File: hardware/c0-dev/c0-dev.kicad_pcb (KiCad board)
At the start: 2 copper layers, 565 parts, among them J1 2913730000, J10 2913730000, J11 2913730000, J12 2913710000, J13 2913730000, J14 2913730000, J15 RJ45_LED_Shielded, J16 TAG_CONNECT, J17 PinHeader_2.54mm, J2 2913710000, J3 2913730000, J4 2913730000, J5 2913710000, J6 2913730000, J7 2913730000, J8 2913710000, J9 2913730000, Q1 BSS138P, Q10 BSS138P, Q2 BSS138P, Q3 BSS138P, Q4 BSS138P, Q5 BSS138P, Q6 BSS138P, Q7 BSS138P, Q8 BSS138P, Q9 BSS138P, U1 LAN8720A, U10 RP2350A, U11 TMP117xxDRV, U12 B0505S-1WR3, U13 ISO1540, U14 AMS1117-3.3, U15 ADS1015IDGS, U16 ADS1015IDGS, U17 B0505S-1WR3, U18 ISO1540, U19 ADS1015IDGS, U2 TPS54360DDA, U20 ADS1015IDGS, U21 ADS1015IDGS, U22 ADS1015IDGS, U23 B0505S-1WR3, U24 ISO6741, U25 ISO6741, U26 ADS1220xPW, U27 ADS1220xPW, U28 B0505S-1WR3, U29 ISO1044BD, U3 TPS2378, U30 TLP175A, U31 ISO1212, U32 ISO1212, U33 ISO1212, U34 ISO1212, U35 B0505S-1WR3, U36 ISO1540, U37 TLP175A, U38 TCA9555PWR, U39 TPS26600PWP, U39 TPS4H000A-Q1, U4 TLP175A, U40 TPS26600PWP, U41 TPS26600PWP, U42 TPS26600PWP, U43 TPS26600PWP, U44 TPS26600PWP, U45 TPS26600PWP, U46 TPS26600PWP, U47 ER_OLEDM0.91_1x-I2C, U47 TPS26600PWP, U48 ER_OLEDM0.91_1x-I2C, U48 TPS4H000A-Q1, U5 B0505S-1WR3, U6 AMS1117-3.3, U7 TCA9555PWR, U8 W25Q128JVP, U9 TPS3820-33DBV, Y1 ABM8-272-T3 (12Mhz)

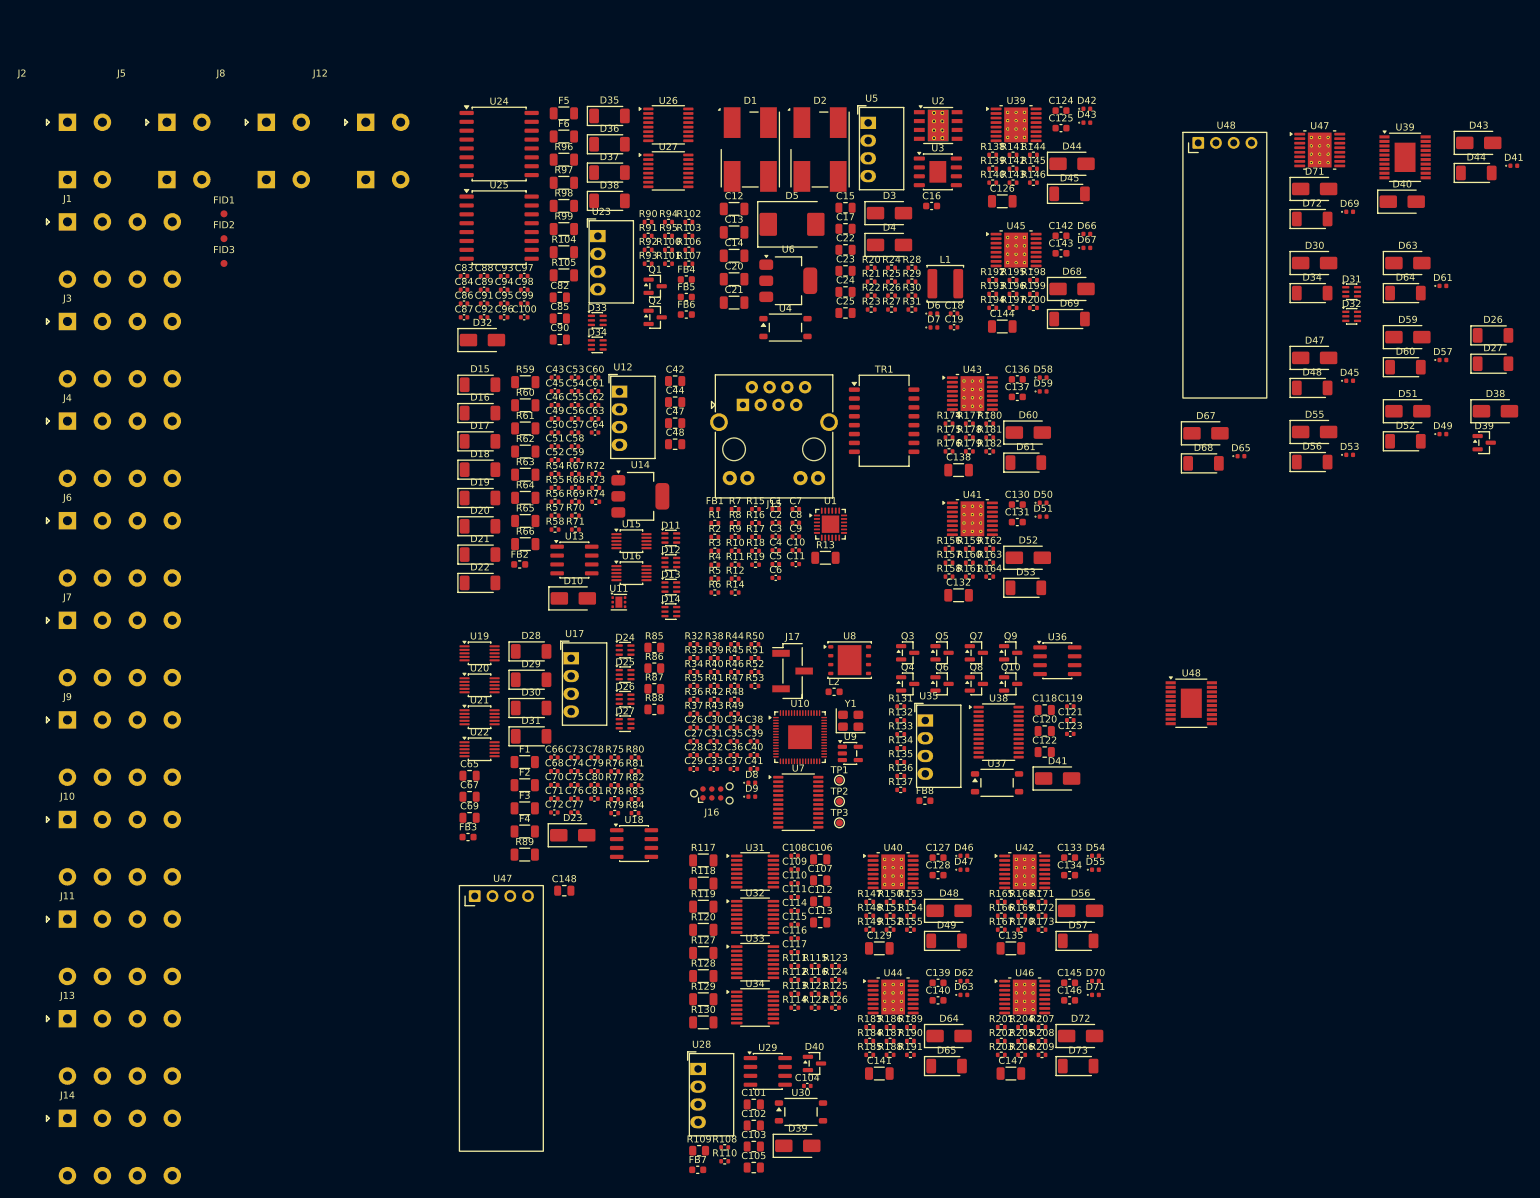
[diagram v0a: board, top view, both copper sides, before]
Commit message: power and isolation cleanup
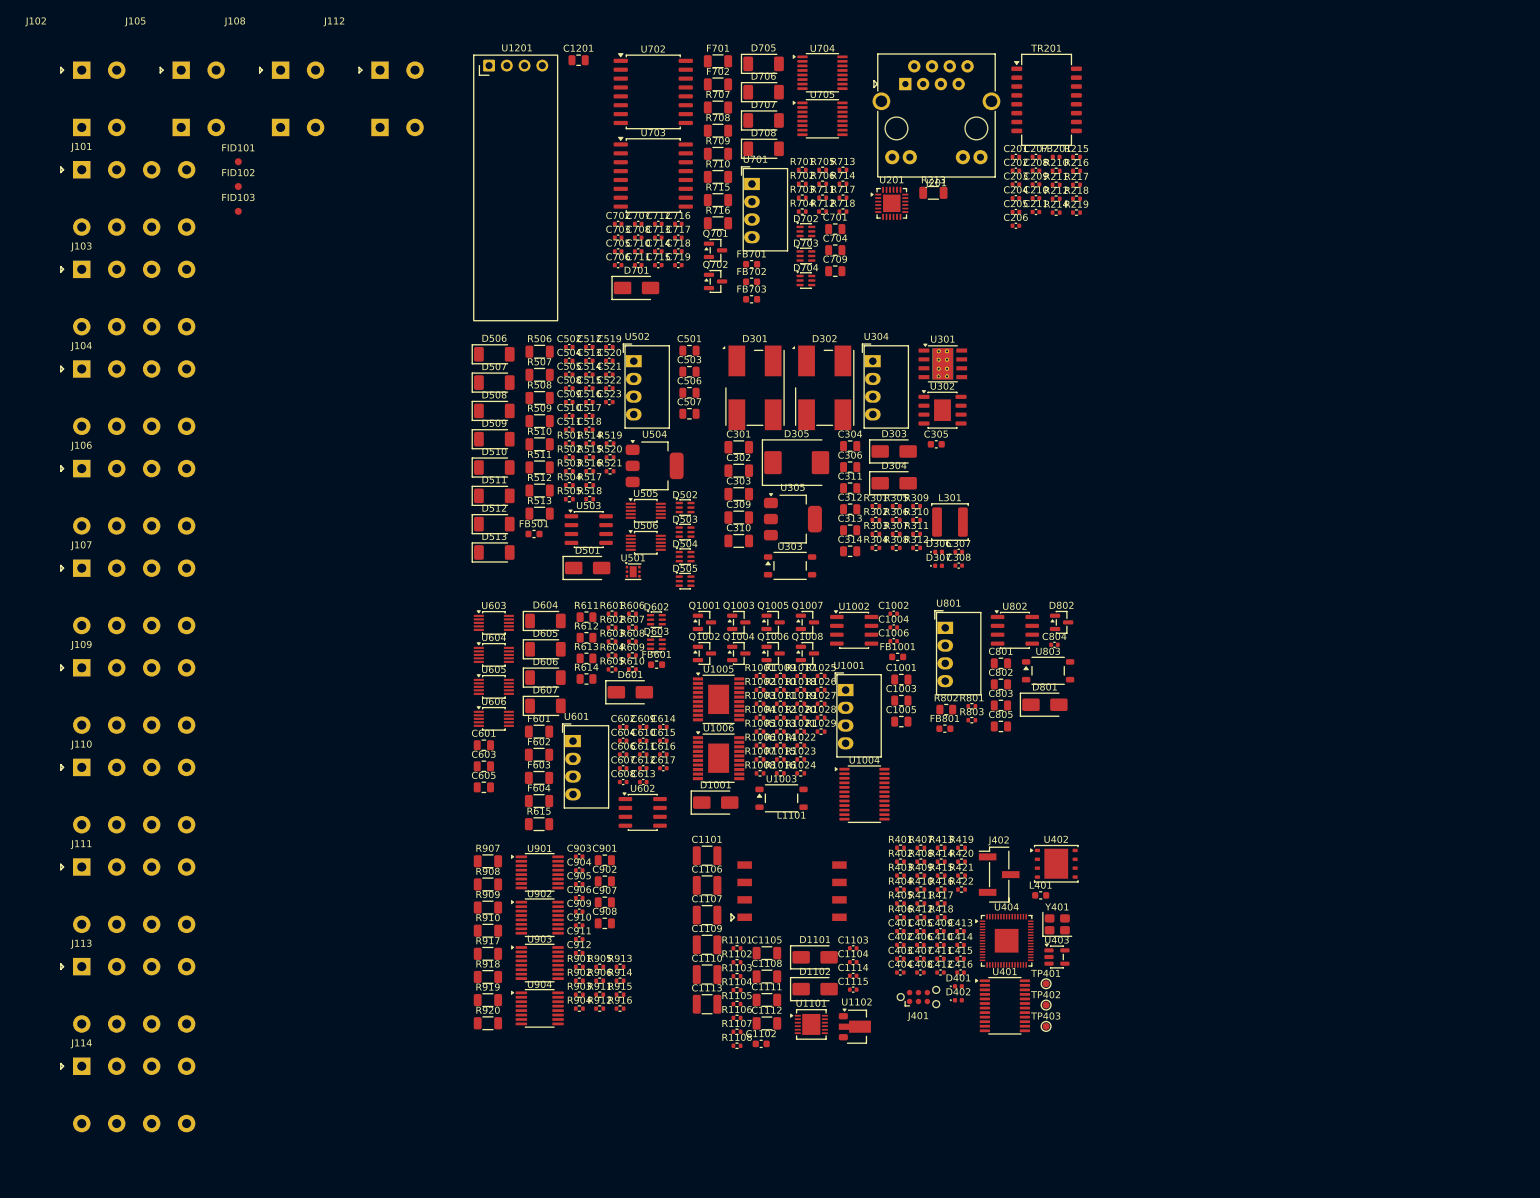
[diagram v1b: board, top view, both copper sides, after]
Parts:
- removed C1, C100, C104, C119, C121, C123, C26, C4, C43, C45, C46, C5, C51, C52, C53, C54, C55, C56, C57, C58, C59, C6, C60, C61, C62, C63, C64, C66, C68, C74, C75, C76, C77, C78, C79, C80, C81, C83, C84, C86, C87, C88, C89, C91, C92, C93, C94, C95, C96, C97, C98, C99: 0.1uF, Capacitor_SMD:C_0402_1005Metric
- removed C10, C11, C7, C8, C9: 22nF, Capacitor_SMD:C_0402_1005Metric
- removed C101, C102, C103, C105, C106, C107, C112, C113, C118, C120, C122, C148, C22, C23, C24, C25, C42, C44, C47, C48, C65, C67, C69, C82, C85, C90: 10uF, Capacitor_SMD:C_0805_2012Metric
- removed C108, C109, C110, C111, C114, C115, C116, C117: 1nF, Capacitor_SMD:C_0402_1005Metric
- removed C12, C13, C14: 1uF, Capacitor_SMD:C_1206_3216Metric
- removed C124, C127, C130, C133, C136, C139, C142, C145: 1uF, Capacitor_SMD:C_0603_1608Metric
- removed C125, C128, C131, C134, C137, C140, C143, C146: 2.2uF, Capacitor_SMD:C_0603_1608Metric
- removed C126, C129, C132, C135, C138, C141, C144, C147: 10uF, Capacitor_SMD:C_1206_3216Metric
- removed C15, C17: 0.1uF, Capacitor_SMD:C_0805_2012Metric
- removed C16: 0.1uF, Capacitor_SMD:C_0603_1608Metric
- removed C18: 270pF, Capacitor_SMD:C_0402_1005Metric
- removed C19: 3.3nF, Capacitor_SMD:C_0402_1005Metric
- removed C2, C49, C50, C70, C71, C72, C73: 1uF, Capacitor_SMD:C_0402_1005Metric
- removed C20, C21: 22uF, Capacitor_SMD:C_1206_3216Metric
- removed C27, C28, C34, C37: 4.7u, Capacitor_SMD:C_0402_1005Metric
- removed C29, C30, C31, C32, C33, C35, C36, C38, C39: 0.1u, Capacitor_SMD:C_0402_1005Metric
- removed C3: 470pF, Capacitor_SMD:C_0402_1005Metric
- removed C40, C41: 15p, Capacitor_SMD:C_0402_1005Metric
- removed D1, D2: CD-DF406SL, Diode_SMD:Diode_Bridge_Bourns_CD-DF4xxS
- removed D10, D23, D30, D32, D38, D39, D4, D40, D41, D43, D44, D47, D48, D51, D52, D55, D56, D59, D60, D63, D64, D67, D68, D71, D72: SS14, Diode_SMD:D_SMA
- removed D11, D12, D13, D14, D24, D25, D26, D27, D31, D32, D33, D34: BAV199DW, Package_TO_SOT_SMD:SOT-363_SC-70-6
- removed D15, D16, D17, D18, D19, D20, D21, D22, D26, D27, D28, D29, D30, D31, D34, D35, D36, D37, D38, D44, D45, D48, D49, D52, D53, D56, D57, D60, D61, D64, D65, D68, D69, D72, D73: PTVS30VP1UP, Diode_SMD:D_SOD-128
- removed D3: SMAJ58A, Diode_SMD:D_SMA
- removed D39, D40: NUP2105L, Package_TO_SOT_SMD:SOT-23
- removed D41, D45, D49, D53, D57, D6, D61, D65, D69, D7, D9: green, LED_SMD:LED_0402_1005Metric
- removed D42, D43, D46, D47, D50, D51, D54, D55, D58, D59, D62, D63, D66, D67, D70, D71, D8: red, LED_SMD:LED_0402_1005Metric
- removed D5: B560C, Diode_SMD:D_SMC
- removed F1, F2, F3, F4, F5, F6: 50mA, Resistor_SMD:R_1206_3216Metric
- removed FB1: 1kΩ@100MHz, Inductor_SMD:L_0402_1005Metric
- removed FB2, FB3, FB4, FB5, FB6, FB7, FB8: 600Ω@100MHz, Inductor_SMD:L_0603_1608Metric
- removed FID1, FID2, FID3: Fiducial, Fiducial:Fiducial_1mm_Mask2mm
- removed J1, J10, J11, J13, J14, J3, J4, J6, J7, J9: 2913730000, conduit:2913730000
- removed J12, J2, J5, J8: 2913710000, conduit:2913710000
- removed J15: RJ45_LED_Shielded, Connector_RJ:RJ45_BEL_SS74301-00x_Vertical
- removed J16: TAG_CONNECT, Connector:Tag-Connect_TC2030-IDC-NL_2x03_P1.27mm_Vertical
- removed J17: PinHeader_2.54mm, Connector_PinHeader_2.54mm:PinHeader_1x03_P2.54mm_Vertical_SMD_Pin1Left
- removed L1: 4.7uH, Inductor_SMD:L_Sunlord_SWPA5040S
- removed L2: 3.3u, Inductor_SMD:L_0603_1608Metric
- removed Q1, Q10, Q2, Q3, Q4, Q5, Q6, Q7, Q8, Q9: BSS138P, Package_TO_SOT_SMD:SOT-23
- removed R1, R137, R144, R153, R162, R171, R180, R189, R198, R207, R28, R35, R46, R90, R91: 10k, Resistor_SMD:R_0402_1005Metric
- removed R10, R11, R12, R9: 49.9R, Resistor_SMD:R_0402_1005Metric
- removed R100, R101, R102, R103, R67, R68, R69, R70, R71, R72, R73, R74: 1M, Resistor_SMD:R_0402_1005Metric
- removed R104, R105, R117, R118, R119, R120, R127, R128, R129, R130, R59, R60, R61, R62, R63, R64, R65, R66, R96, R97, R98, R99: 2k, Resistor_SMD:R_1206_3216Metric
- removed R106, R107, R110, R143, R152, R161, R170, R179, R188, R197, R206, R21, R42: 0, Resistor_SMD:R_0402_1005Metric
- removed R108, R111, R112, R121, R122, R131, R132, R133, R134, R135, R136, R141, R142, R150, R151, R159, R160, R168, R169, R177, R178, R186, R187, R195, R196, R2, R204, R205, R27, R29, R30, R31, R32, R33, R34, R37, R38, R39, R40, R43, R45, R48, R49, R50, R51, R52, R53, R54, R55, R56, R57, R58, R75, R76, R77, R78, R79, R80, R92, R93, R94, R95: 1k, Resistor_SMD:R_0402_1005Metric
- removed R109: 120R, Resistor_SMD:R_0805_2012Metric
- removed R113, R114, R115, R116, R123, R124, R125, R126: 560, Resistor_SMD:R_0402_1005Metric
- removed R13: 2M, Resistor_SMD:R_1206_3216Metric
- removed R138, R147, R156, R165, R174, R183, R192, R201: 715k, Resistor_SMD:R_0402_1005Metric
- removed R139, R148, R157, R166, R175, R184, R193, R202: 20k, Resistor_SMD:R_0402_1005Metric
- removed R14, R15, R16, R17: 75R, Resistor_SMD:R_0402_1005Metric
- removed R140, R149, R158, R167, R176, R185, R194, R203: 30.1k, Resistor_SMD:R_0402_1005Metric
- removed R145, R154, R163, R172, R181, R190, R199, R208: 12k, Resistor_SMD:R_0402_1005Metric
- removed R146, R155, R164, R173, R182, R191, R200, R209: 62k, Resistor_SMD:R_0402_1005Metric
- removed R18, R19, R7: 33R, Resistor_SMD:R_0402_1005Metric
- removed R20: 68.1k, Resistor_SMD:R_0402_1005Metric
- removed R22: 25k, Resistor_SMD:R_0402_1005Metric
- removed R23: 63.4R, Resistor_SMD:R_0402_1005Metric
- removed R24: 6.34k, Resistor_SMD:R_0402_1005Metric
- removed R25: 60.4k, Resistor_SMD:R_0402_1005Metric
- removed R26: 11.5k, Resistor_SMD:R_0402_1005Metric
- removed R3, R4, R5, R6: 10R, Resistor_SMD:R_0402_1005Metric
- removed R36: 33, Resistor_SMD:R_0402_1005Metric
- removed R41: DNP, Resistor_SMD:R_0402_1005Metric
- removed R44, R47: 27, Resistor_SMD:R_0402_1005Metric
- removed R8: 12.1k, Resistor_SMD:R_0402_1005Metric
- removed R81, R82, R83, R84: 1.6k, Resistor_SMD:R_0402_1005Metric
- removed R85, R86, R87, R88: 160, Resistor_SMD:R_0805_2012Metric
- removed R89: 0, Resistor_SMD:R_1206_3216Metric
- removed TP1, TP2, TP3: 1mm, TestPoint:TestPoint_Pad_D1.0mm
- removed TR1: TS8121CMHF, conduit:Transformer_Ethernet_Bourns_PT61017PEL
- removed U1: LAN8720A, conduit:VQFN-24-1EP_4x4mm_P0.5mm_EP2.5x2.5mm
- removed U10: RP2350A, Package_DFN_QFN:QFN-60-1EP_7x7mm_P0.4mm_EP3.4x3.4mm
- removed U11: TMP117xxDRV, Package_SON:WSON-6-1EP_2x2mm_P0.65mm_EP1x1.6mm
- removed U12, U17, U23, U28, U35, U5: B0505S-1WR3, Converter_DCDC:Converter_DCDC_Murata_MEE1SxxxxSC_THT
- removed U13, U18, U36: ISO1540, Package_SO:SOIC-8_3.9x4.9mm_P1.27mm
- removed U14, U6: AMS1117-3.3, Package_TO_SOT_SMD:SOT-223-3_TabPin2
- removed U15, U16, U19, U20, U21, U22: ADS1015IDGS, Package_SO:TSSOP-10_3x3mm_P0.5mm
- removed U2: TPS54360DDA, Package_SO:TI_SO-PowerPAD-8_ThermalVias
- removed U24, U25: ISO6741, Package_SO:SOIC-16W_7.5x10.3mm_P1.27mm
- removed U26, U27: ADS1220xPW, Package_SO:TSSOP-16_4.4x5mm_P0.65mm
- removed U29: ISO1044BD, Package_SO:SOIC-8_3.9x4.9mm_P1.27mm
- removed U3: TPS2378, Package_SO:HSOP-8-1EP_3.9x4.9mm_P1.27mm_EP2.41x3.1mm
- removed U30, U37, U4: TLP175A, Package_SO:Toshiba_SOIC-4-6_4.4x3.6mm_P1.27mm
- removed U31, U32, U33, U34: ISO1212, Package_SO:SSOP-16_3.9x4.9mm_P0.635mm
- removed U38, U7: TCA9555PWR, Package_SO:TSSOP-24_4.4x7.8mm_P0.65mm
- removed U39, U48: TPS4H000A-Q1, Package_SO:ETSSOP-20-1EP_4.4x6.5mm_P0.65mm_EP3x4.2mm
- removed U39, U40, U41, U42, U43, U44, U45, U46, U47: TPS26600PWP, Package_SO:HTSSOP-16-1EP_4.4x5mm_P0.65mm_EP3.4x5mm_Mask2.66x2.46mm_ThermalVias
- removed U47, U48: ER_OLEDM0.91_1x-I2C, Display:ER_OLEDM0.91_1x-I2C
- removed U8: W25Q128JVP, Package_SON:WSON-8-1EP_6x5mm_P1.27mm_EP3.4x4.3mm
- removed U9: TPS3820-33DBV, Package_TO_SOT_SMD:SOT-23-5
- removed Y1: ABM8-272-T3 (12Mhz), Crystal:Crystal_SMD_Abracon_ABM8G-4Pin_3.2x2.5mm
- added C1001: 10uF, Capacitor_SMD:C_0805_2012Metric, F.Cu at (150.9, 114.0)
- added C1002: 0.1uF, Capacitor_SMD:C_0402_1005Metric, F.Cu at (149.8, 104.6)
- added C1003: 10uF, Capacitor_SMD:C_0805_2012Metric, F.Cu at (150.9, 117.1)
- added C1004: 0.1uF, Capacitor_SMD:C_0402_1005Metric, F.Cu at (149.8, 106.6)
- added C1005: 10uF, Capacitor_SMD:C_0805_2012Metric, F.Cu at (150.9, 120.1)
- added C1006: 0.1uF, Capacitor_SMD:C_0402_1005Metric, F.Cu at (149.8, 108.6)
- added C1101: 10uF, Capacitor_SMD:C_1210_3225Metric, F.Cu at (123.1, 139.2)
- added C1102: 0.1uF, Capacitor_SMD:C_0603_1608Metric, F.Cu at (130.8, 166.2)
- added C1103: 10nF, Capacitor_SMD:C_0402_1005Metric, F.Cu at (144.0, 152.5)
- added C1104: 10nF, Capacitor_SMD:C_0402_1005Metric, F.Cu at (144.0, 154.5)
- added C1105: 1uF, Capacitor_SMD:C_1206_3216Metric, F.Cu at (131.7, 153.2)
- added C1106: 10uF, Capacitor_SMD:C_1210_3225Metric, F.Cu at (123.1, 143.5)
- added C1107: 10uF, Capacitor_SMD:C_1210_3225Metric, F.Cu at (123.1, 147.8)
- added C1108: 1uF, Capacitor_SMD:C_1206_3216Metric, F.Cu at (131.7, 156.5)
- added C1109: 10uF, Capacitor_SMD:C_1210_3225Metric, F.Cu at (123.1, 152.0)
- added C1110: 10uF, Capacitor_SMD:C_1210_3225Metric, F.Cu at (123.1, 156.2)
- added C1111: 1uF, Capacitor_SMD:C_1206_3216Metric, F.Cu at (131.7, 159.9)
- added C1112: 1uF, Capacitor_SMD:C_1206_3216Metric, F.Cu at (131.7, 163.2)
- added C1113: 10uF, Capacitor_SMD:C_1210_3225Metric, F.Cu at (123.1, 160.5)
- added C1114: 10nF, Capacitor_SMD:C_0402_1005Metric, F.Cu at (144.0, 156.4)
- added C1115: 4.7nF, Capacitor_SMD:C_0402_1005Metric, F.Cu at (144.0, 158.4)
- added C1201: 10uF, Capacitor_SMD:C_0805_2012Metric, F.Cu at (104.7, 25.4)
- added C201: 0.1uF, Capacitor_SMD:C_0402_1005Metric, F.Cu at (167.3, 39.3)
- added C202: 1uF, Capacitor_SMD:C_0402_1005Metric, F.Cu at (167.3, 41.2)
- added C203: 470pF, Capacitor_SMD:C_0402_1005Metric, F.Cu at (167.3, 43.2)
- added C204: 0.1uF, Capacitor_SMD:C_0402_1005Metric, F.Cu at (167.3, 45.2)
- added C205: 0.1uF, Capacitor_SMD:C_0402_1005Metric, F.Cu at (167.3, 47.2)
- added C206: 0.1uF, Capacitor_SMD:C_0402_1005Metric, F.Cu at (167.3, 49.1)
- added C207: 22nF, Capacitor_SMD:C_0402_1005Metric, F.Cu at (170.2, 39.3)
- added C208: 22nF, Capacitor_SMD:C_0402_1005Metric, F.Cu at (170.2, 41.2)
- added C209: 22nF, Capacitor_SMD:C_0402_1005Metric, F.Cu at (170.2, 43.2)
- added C210: 22nF, Capacitor_SMD:C_0402_1005Metric, F.Cu at (170.2, 45.2)
- added C211: 22nF, Capacitor_SMD:C_0402_1005Metric, F.Cu at (170.2, 47.2)
- added C301: 1uF, Capacitor_SMD:C_1206_3216Metric, F.Cu at (127.6, 80.8)
- added C302: 1uF, Capacitor_SMD:C_1206_3216Metric, F.Cu at (127.6, 84.2)
- added C303: 1uF, Capacitor_SMD:C_1206_3216Metric, F.Cu at (127.6, 87.5)
- added C304: 0.1uF, Capacitor_SMD:C_0805_2012Metric, F.Cu at (143.6, 80.7)
- added C305: 0.1uF, Capacitor_SMD:C_0603_1608Metric, F.Cu at (155.9, 80.4)
- added C306: 0.1uF, Capacitor_SMD:C_0805_2012Metric, F.Cu at (143.6, 83.7)
- added C307: 270pF, Capacitor_SMD:C_0402_1005Metric, F.Cu at (159.1, 95.8)
- added C308: 3.3nF, Capacitor_SMD:C_0402_1005Metric, F.Cu at (159.1, 97.8)
- added C309: 22uF, Capacitor_SMD:C_1206_3216Metric, F.Cu at (127.6, 90.9)
- added C310: 22uF, Capacitor_SMD:C_1206_3216Metric, F.Cu at (127.6, 94.2)
- added C311: 10uF, Capacitor_SMD:C_0805_2012Metric, F.Cu at (143.6, 86.7)
- added C312: 10uF, Capacitor_SMD:C_0805_2012Metric, F.Cu at (143.6, 89.7)
- added C313: 10uF, Capacitor_SMD:C_0805_2012Metric, F.Cu at (143.6, 92.7)
- added C314: 10uF, Capacitor_SMD:C_0805_2012Metric, F.Cu at (143.6, 95.7)
- added C401: 0.1uF, Capacitor_SMD:C_0402_1005Metric, F.Cu at (150.8, 150.1)
- added C402: 4.7u, Capacitor_SMD:C_0402_1005Metric, F.Cu at (150.8, 152.0)
- added C403: 4.7u, Capacitor_SMD:C_0402_1005Metric, F.Cu at (150.8, 154.0)
- added C404: 0.1u, Capacitor_SMD:C_0402_1005Metric, F.Cu at (150.8, 156.0)
- added C405: 0.1u, Capacitor_SMD:C_0402_1005Metric, F.Cu at (153.6, 150.1)
- added C406: 0.1u, Capacitor_SMD:C_0402_1005Metric, F.Cu at (153.6, 152.0)
- added C407: 0.1u, Capacitor_SMD:C_0402_1005Metric, F.Cu at (153.6, 154.0)
- added C408: 0.1u, Capacitor_SMD:C_0402_1005Metric, F.Cu at (153.6, 156.0)
- added C409: 4.7u, Capacitor_SMD:C_0402_1005Metric, F.Cu at (156.5, 150.1)
- added C410: 0.1u, Capacitor_SMD:C_0402_1005Metric, F.Cu at (156.5, 152.0)
- added C411: 0.1u, Capacitor_SMD:C_0402_1005Metric, F.Cu at (156.5, 154.0)
- added C412: 4.7u, Capacitor_SMD:C_0402_1005Metric, F.Cu at (156.5, 156.0)
- added C413: 0.1u, Capacitor_SMD:C_0402_1005Metric, F.Cu at (159.4, 150.1)
- added C414: 0.1u, Capacitor_SMD:C_0402_1005Metric, F.Cu at (159.4, 152.0)
- added C415: 15p, Capacitor_SMD:C_0402_1005Metric, F.Cu at (159.4, 154.0)
- added C416: 15p, Capacitor_SMD:C_0402_1005Metric, F.Cu at (159.4, 156.0)
- added C501: 10uF, Capacitor_SMD:C_0805_2012Metric, F.Cu at (120.6, 67.0)
- added C502: 0.1uF, Capacitor_SMD:C_0402_1005Metric, F.Cu at (103.4, 66.5)
- added C503: 10uF, Capacitor_SMD:C_0805_2012Metric, F.Cu at (120.6, 70.0)
- added C504: 0.1uF, Capacitor_SMD:C_0402_1005Metric, F.Cu at (103.4, 68.5)
- added C505: 0.1uF, Capacitor_SMD:C_0402_1005Metric, F.Cu at (103.4, 70.4)
- added C506: 10uF, Capacitor_SMD:C_0805_2012Metric, F.Cu at (120.6, 73.0)
- added C507: 10uF, Capacitor_SMD:C_0805_2012Metric, F.Cu at (120.6, 76.0)
- added C508: 1uF, Capacitor_SMD:C_0402_1005Metric, F.Cu at (103.4, 72.4)
- added C509: 1uF, Capacitor_SMD:C_0402_1005Metric, F.Cu at (103.4, 74.4)
- added C510: 0.1uF, Capacitor_SMD:C_0402_1005Metric, F.Cu at (103.4, 76.3)
- added C511: 0.1uF, Capacitor_SMD:C_0402_1005Metric, F.Cu at (103.4, 78.3)
- added C512: 0.1uF, Capacitor_SMD:C_0402_1005Metric, F.Cu at (106.3, 66.5)
- added C513: 0.1uF, Capacitor_SMD:C_0402_1005Metric, F.Cu at (106.3, 68.5)
- added C514: 0.1uF, Capacitor_SMD:C_0402_1005Metric, F.Cu at (106.3, 70.4)
- added C515: 0.1uF, Capacitor_SMD:C_0402_1005Metric, F.Cu at (106.3, 72.4)
- added C516: 0.1uF, Capacitor_SMD:C_0402_1005Metric, F.Cu at (106.3, 74.4)
- added C517: 0.1uF, Capacitor_SMD:C_0402_1005Metric, F.Cu at (106.3, 76.3)
- added C518: 0.1uF, Capacitor_SMD:C_0402_1005Metric, F.Cu at (106.3, 78.3)
- added C519: 0.1uF, Capacitor_SMD:C_0402_1005Metric, F.Cu at (109.1, 66.5)
- added C520: 0.1uF, Capacitor_SMD:C_0402_1005Metric, F.Cu at (109.1, 68.5)
- added C521: 0.1uF, Capacitor_SMD:C_0402_1005Metric, F.Cu at (109.1, 70.4)
- added C522: 0.1uF, Capacitor_SMD:C_0402_1005Metric, F.Cu at (109.1, 72.4)
- added C523: 0.1uF, Capacitor_SMD:C_0402_1005Metric, F.Cu at (109.1, 74.4)
- added C601: 10uF, Capacitor_SMD:C_0805_2012Metric, F.Cu at (91.2, 123.5)
- added C602: 0.1uF, Capacitor_SMD:C_0402_1005Metric, F.Cu at (111.1, 120.8)
- added C603: 10uF, Capacitor_SMD:C_0805_2012Metric, F.Cu at (91.2, 126.5)
- added C604: 0.1uF, Capacitor_SMD:C_0402_1005Metric, F.Cu at (111.1, 122.8)
- added C605: 10uF, Capacitor_SMD:C_0805_2012Metric, F.Cu at (91.2, 129.5)
- added C606: 1uF, Capacitor_SMD:C_0402_1005Metric, F.Cu at (111.1, 124.8)
- added C607: 1uF, Capacitor_SMD:C_0402_1005Metric, F.Cu at (111.1, 126.7)
- added C608: 1uF, Capacitor_SMD:C_0402_1005Metric, F.Cu at (111.1, 128.7)
- added C609: 1uF, Capacitor_SMD:C_0402_1005Metric, F.Cu at (114.0, 120.8)
- added C610: 0.1uF, Capacitor_SMD:C_0402_1005Metric, F.Cu at (114.0, 122.8)
- added C611: 0.1uF, Capacitor_SMD:C_0402_1005Metric, F.Cu at (114.0, 124.8)
- added C612: 0.1uF, Capacitor_SMD:C_0402_1005Metric, F.Cu at (114.0, 126.7)
- added C613: 0.1uF, Capacitor_SMD:C_0402_1005Metric, F.Cu at (114.0, 128.7)
- added C614: 0.1uF, Capacitor_SMD:C_0402_1005Metric, F.Cu at (116.8, 120.8)
- added C615: 0.1uF, Capacitor_SMD:C_0402_1005Metric, F.Cu at (116.8, 122.8)
- added C616: 0.1uF, Capacitor_SMD:C_0402_1005Metric, F.Cu at (116.8, 124.8)
- added C617: 0.1uF, Capacitor_SMD:C_0402_1005Metric, F.Cu at (116.8, 126.7)
- added C701: 10uF, Capacitor_SMD:C_0805_2012Metric, F.Cu at (141.4, 49.6)
- added C702: 0.1uF, Capacitor_SMD:C_0402_1005Metric, F.Cu at (110.4, 48.9)
- added C703: 0.1uF, Capacitor_SMD:C_0402_1005Metric, F.Cu at (110.4, 50.8)
- added C704: 10uF, Capacitor_SMD:C_0805_2012Metric, F.Cu at (141.4, 52.6)
- added C705: 0.1uF, Capacitor_SMD:C_0402_1005Metric, F.Cu at (110.4, 52.8)
- added C706: 0.1uF, Capacitor_SMD:C_0402_1005Metric, F.Cu at (110.4, 54.8)
- added C707: 0.1uF, Capacitor_SMD:C_0402_1005Metric, F.Cu at (113.3, 48.9)
- added C708: 0.1uF, Capacitor_SMD:C_0402_1005Metric, F.Cu at (113.3, 50.8)
- added C709: 10uF, Capacitor_SMD:C_0805_2012Metric, F.Cu at (141.4, 55.6)
- added C710: 0.1uF, Capacitor_SMD:C_0402_1005Metric, F.Cu at (113.3, 52.8)
- added C711: 0.1uF, Capacitor_SMD:C_0402_1005Metric, F.Cu at (113.3, 54.8)
- added C712: 0.1uF, Capacitor_SMD:C_0402_1005Metric, F.Cu at (116.1, 48.9)
- added C713: 0.1uF, Capacitor_SMD:C_0402_1005Metric, F.Cu at (116.1, 50.8)
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
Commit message: cjc overhaul
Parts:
- removed C1002, C1004, C1006, C613, C614, C615, C616, C617: 0.1uF, Capacitor_SMD:C_0402_1005Metric
- removed C1003, C1005: 10uF, Capacitor_SMD:C_0805_2012Metric
- removed D1001: SS14, Diode_SMD:D_SMA
- removed D607: PTVS30VP1UP, Diode_SMD:D_SOD-128
- removed FB1001, FB601: 600Ω@100MHz, Inductor_SMD:L_0603_1608Metric
- removed J110: 2913730000, conduit:2913730000
- removed R615: 0, Resistor_SMD:R_1206_3216Metric
- removed U1004: TCA9555PWR, Package_SO:TSSOP-24_4.4x7.8mm_P0.65mm
- removed U1005, U1006: TPS4H000A-Q1, Package_SO:ETSSOP-20-1EP_4.4x6.5mm_P0.65mm_EP3x4.2mm
- removed U305: AMS1117-3.3, Package_TO_SOT_SMD:SOT-223-3_TabPin2
- removed U605, U606: ADS1015IDGS, Package_SO:TSSOP-10_3x3mm_P0.5mm
- added C1116: 4.7nF, Capacitor_SMD:C_0402_1005Metric, F.Cu at (133.4, 125.0)
- added C315: 3.3nF, Capacitor_SMD:C_0402_1005Metric, F.Cu at (133.4, 69.0)
- added C316: 22uF, Capacitor_SMD:C_1206_3216Metric, F.Cu at (112.5, 54.3)
- added C317: 22uF, Capacitor_SMD:C_1206_3216Metric, F.Cu at (112.5, 57.7)
- added C318: 100uF, Capacitor_Tantalum_SMD:CP_EIA-3528-21_Kemet-B, F.Cu at (118.4, 65.2)
- added C524: 0.1uF, Capacitor_SMD:C_0402_1005Metric, F.Cu at (51.0, 134.2)
- added C525: 0.1uF, Capacitor_SMD:C_0402_1005Metric, F.Cu at (51.0, 136.2)
- added L302: 4.7uH, Inductor_SMD:L_Sunlord_SWPA5040S, F.Cu at (135.3, 60.8)
- added Q1009: BSS138P, Package_TO_SOT_SMD:SOT-23, F.Cu at (151.3, 114.8)
- added R1030: 20k, Resistor_SMD:R_0402_1005Metric, F.Cu at (152.1, 128.0)
- added R1109: 51k, Resistor_SMD:R_0402_1005Metric, F.Cu at (122.5, 133.0)
- added R1301: 1k, Resistor_SMD:R_0402_1005Metric, F.Cu at (131.2, 168.1)
- added R1302: 1k, Resistor_SMD:R_0402_1005Metric, F.Cu at (131.2, 170.1)
- added R1303: 1k, Resistor_SMD:R_0402_1005Metric, F.Cu at (131.2, 172.1)
- added R1304: 1k, Resistor_SMD:R_0402_1005Metric, F.Cu at (131.2, 174.1)
- added R1305: 2.4k, Resistor_SMD:R_0402_1005Metric, F.Cu at (131.2, 176.0)
- added R1306: 1k, Resistor_SMD:R_0402_1005Metric, F.Cu at (134.1, 168.1)
- added R1307: 1k, Resistor_SMD:R_0402_1005Metric, F.Cu at (134.1, 170.1)
- added R1308: 4.7k, Resistor_SMD:R_0402_1005Metric, F.Cu at (134.1, 172.1)
- added R1309: 20k, Resistor_SMD:R_0402_1005Metric, F.Cu at (134.1, 174.1)
- added R1310: 20k, Resistor_SMD:R_0402_1005Metric, F.Cu at (134.1, 176.0)
- added R201: 10k, Resistor_SMD:R_0402_1005Metric, F.Cu at (131.0, 90.7)
- added R202: 1k, Resistor_SMD:R_0402_1005Metric, F.Cu at (131.0, 92.7)
- added R203: 10R, Resistor_SMD:R_0402_1005Metric, F.Cu at (131.0, 94.7)
- added R204: 10R, Resistor_SMD:R_0402_1005Metric, F.Cu at (131.0, 96.7)
- added R205: 10R, Resistor_SMD:R_0402_1005Metric, F.Cu at (131.0, 98.7)
- added R206: 10R, Resistor_SMD:R_0402_1005Metric, F.Cu at (131.0, 100.7)
- added R207: 33R, Resistor_SMD:R_0402_1005Metric, F.Cu at (133.9, 88.7)
- added R208: 12.1k, Resistor_SMD:R_0402_1005Metric, F.Cu at (133.9, 90.7)
- added R209: 49.9R, Resistor_SMD:R_0402_1005Metric, F.Cu at (133.9, 92.7)
- added R522: 1M, Resistor_SMD:R_0402_1005Metric, F.Cu at (51.1, 140.2)
- added R523: 1M, Resistor_SMD:R_0402_1005Metric, F.Cu at (51.1, 142.2)
- added U1301: TPS4H000A-Q1, Package_SO:ETSSOP-20-1EP_4.4x6.5mm_P0.65mm_EP3x4.2mm, F.Cu at (140.0, 171.4)
- added U507: ADS1015IDGS, Package_SO:TSSOP-10_3x3mm_P0.5mm, F.Cu at (64.6, 152.4)
- C1001, C503, C507, C605: value 10uF -> 0.1uF; footprint Capacitor_SMD:C_0805_2012Metric -> Capacitor_SMD:C_0402_1005Metric
- C1113: value 10uF -> 1nF; footprint Capacitor_SMD:C_1210_3225Metric -> Capacitor_SMD:C_1206_3216Metric
- C1114: value 10nF -> 10uF; footprint Capacitor_SMD:C_0402_1005Metric -> Capacitor_SMD:C_1210_3225Metric
- C1115: value 4.7nF -> 10nF
- C208, C209, C210, C211: value 22nF -> 1nF; footprint Capacitor_SMD:C_0402_1005Metric -> Capacitor_SMD:C_1206_3216Metric
- C301, C303: value 1uF -> 10uF; footprint Capacitor_SMD:C_1206_3216Metric -> Capacitor_SMD:C_1210_3225Metric
- C302: value 1uF -> 22uF
- C304: value 0.1uF -> 10uF; footprint Capacitor_SMD:C_0805_2012Metric -> Capacitor_SMD:C_1210_3225Metric
- C306: value 0.1uF -> 1uF; footprint Capacitor_SMD:C_0805_2012Metric -> Capacitor_SMD:C_1206_3216Metric
- C307: value 270pF -> 1uF; footprint Capacitor_SMD:C_0402_1005Metric -> Capacitor_SMD:C_1206_3216Metric
- C308: value 3.3nF -> 0.1uF
- C309: value 22uF -> 1uF
- C310: value 22uF -> 0.1uF; footprint Capacitor_SMD:C_1206_3216Metric -> Capacitor_SMD:C_0805_2012Metric
- C311: value 10uF -> 22uF; footprint Capacitor_SMD:C_0805_2012Metric -> Capacitor_SMD:C_1206_3216Metric
- C312: value 10uF -> 100uF; footprint Capacitor_SMD:C_0805_2012Metric -> Capacitor_Tantalum_SMD:CP_EIA-3528-21_Kemet-B
- C313: value 10uF -> 0.1uF
- C314: value 10uF -> 270pF; footprint Capacitor_SMD:C_0805_2012Metric -> Capacitor_SMD:C_0402_1005Metric
- C504: value 0.1uF -> 10uF; footprint Capacitor_SMD:C_0402_1005Metric -> Capacitor_SMD:C_0805_2012Metric
- C508: value 1uF -> 10uF; footprint Capacitor_SMD:C_0402_1005Metric -> Capacitor_SMD:C_0805_2012Metric
- C510, C602, C604: value 0.1uF -> 1uF
- C601, C603: value 10uF -> 1uF; footprint Capacitor_SMD:C_0805_2012Metric -> Capacitor_SMD:C_0402_1005Metric
- C606, C607, C608, C609: value 1uF -> 0.1uF
- D301: value CD-DF406SL -> PTVS30VP1UP; footprint Diode_SMD:Diode_Bridge_Bourns_CD-DF4xxS -> Diode_SMD:D_SOD-128
- D302: value CD-DF406SL -> SS14; footprint Diode_SMD:Diode_Bridge_Bourns_CD-DF4xxS -> Diode_SMD:D_SMA
- D303: value SMAJ58A -> CD-DF406SL; footprint Diode_SMD:D_SMA -> Diode_SMD:Diode_Bridge_Bourns_CD-DF4xxS
- D304: value SS14 -> CD-DF406SL; footprint Diode_SMD:D_SMA -> Diode_SMD:Diode_Bridge_Bourns_CD-DF4xxS
- D305: value B560C -> SMAJ58A; footprint Diode_SMD:D_SMC -> Diode_SMD:D_SMA
- D307: value green -> B560C; footprint LED_SMD:LED_0402_1005Metric -> Diode_SMD:D_SMC
- D601: value SS14 -> BAV199DW; footprint Diode_SMD:D_SMA -> Package_TO_SOT_SMD:SOT-363_SC-70-6
- D603: value BAV199DW -> PTVS30VP1UP; footprint Package_TO_SOT_SMD:SOT-363_SC-70-6 -> Diode_SMD:D_SOD-128
- J105, J108, J112: value 2913710000 -> 2913730000; footprint conduit:2913710000 -> conduit:2913730000
- J106: value 2913730000 -> 2913710000; footprint conduit:2913730000 -> conduit:2913710000
- L301: value 4.7uH -> 2.2uH; footprint Inductor_SMD:L_Sunlord_SWPA5040S -> Inductor_SMD:L_1008_2520Metric
- R1001, R1002, R1009, R1012: value 1k -> 4.7k
- R1007: value 10k -> 1k
- R1008: value 4.7k -> 10k
- R1011: value 4.7k -> 1k
- R1022: value 20k -> 1k
- R1106: value 27k -> 2M; footprint Resistor_SMD:R_0402_1005Metric -> Resistor_SMD:R_1206_3216Metric
- R1107: value 2.4k -> 27k
- R1108: value 51k -> 2.4k
- R301: value 68.1k -> 1k
- R302: value 0 -> 25k
- R303: value 25k -> 63.4R
- R304: value 63.4R -> 68.1k
- R305: value 6.34k -> 1k
- R306: value 60.4k -> 1k
- R307: value 11.5k -> 10k
- R309: value 10k -> 6.34k
- R310: value 1k -> 60.4k
- R311: value 1k -> 11.5k
- R506, R507: value 2k -> 1k; footprint Resistor_SMD:R_1206_3216Metric -> Resistor_SMD:R_0402_1005Metric
- R514, R515: value 1M -> 2k; footprint Resistor_SMD:R_0402_1005Metric -> Resistor_SMD:R_1206_3216Metric
- R611, R612, R613, R614: value 160 -> 82
- U1001: value B0505S-1WR3 -> TCA9555PWR; footprint Converter_DCDC:Converter_DCDC_Murata_MEE1SxxxxSC_THT -> Package_SO:TSSOP-24_4.4x7.8mm_P0.65mm
- U1002: value ISO1540 -> TPS4H000A-Q1; footprint Package_SO:SOIC-8_3.9x4.9mm_P1.27mm -> Package_SO:ETSSOP-20-1EP_4.4x6.5mm_P0.65mm_EP3x4.2mm
- U1003: value TLP175A -> TPS4H000A-Q1; footprint Package_SO:Toshiba_SOIC-4-6_4.4x3.6mm_P1.27mm -> Package_SO:ETSSOP-20-1EP_4.4x6.5mm_P0.65mm_EP3x4.2mm
- U301: value TPS54360DDA -> AP63203WU; footprint Package_SO:TI_SO-PowerPAD-8_ThermalVias -> Package_TO_SOT_SMD:TSOT-23-6
- U303: value TLP175A -> TPS54360DDA; footprint Package_SO:Toshiba_SOIC-4-6_4.4x3.6mm_P1.27mm -> Package_SO:TI_SO-PowerPAD-8_ThermalVias
- U304: value B0505S-1WR3 -> TLP175A; footprint Converter_DCDC:Converter_DCDC_Murata_MEE1SxxxxSC_THT -> Package_SO:Toshiba_SOIC-4-6_4.4x3.6mm_P1.27mm
- U501: value TMP117xxDRV -> B0505S-1WR3; footprint Package_SON:WSON-6-1EP_2x2mm_P0.65mm_EP1x1.6mm -> Converter_DCDC:Converter_DCDC_Murata_MEE1SxxxxSC_THT
- U502: value B0505S-1WR3 -> ISO1540; footprint Converter_DCDC:Converter_DCDC_Murata_MEE1SxxxxSC_THT -> Package_SO:SOIC-8_3.9x4.9mm_P1.27mm
- U505: value ADS1015IDGS -> TMP117xxDRV; footprint Package_SO:TSSOP-10_3x3mm_P0.5mm -> Package_SON:WSON-6-1EP_2x2mm_P0.65mm_EP1x1.6mm
- U601: value B0505S-1WR3 -> ADS1015IDGS; footprint Converter_DCDC:Converter_DCDC_Murata_MEE1SxxxxSC_THT -> Package_SO:TSSOP-10_3x3mm_P0.5mm
- U602: value ISO1540 -> ADS1015IDGS; footprint Package_SO:SOIC-8_3.9x4.9mm_P1.27mm -> Package_SO:TSSOP-10_3x3mm_P0.5mm
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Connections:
- net /frontend_temp/+5V renamed /frontend_temp/+5V_ISO
- C1001 pad 1: +5V_ISO -> +3.3V
- C1001 pad 2: GND_ISO -> GND
- C1101 pad 2: GND_ISO -> /Power/GND_ISO
- C1102 pad 2: GND_ISO -> /Power/GND_ISO
- C1103 pad 2: GND_ISO -> /Power/GND_ISO
- C1105 pad 2: GND_ISO -> /Power/GND_ISO
- C1106 pad 1: /Power/FlyBuck/+24V -> +24V
- C1106 pad 2: /Power/FlyBuck/GND -> GND
- C1107 pad 1: /Power/FlyBuck/+24V -> +24V
- C1107 pad 2: /Power/FlyBuck/GND -> GND
- C1108 pad 1: /Power/FlyBuck/+24V -> +24V
- C1108 pad 2: /Power/FlyBuck/GND -> GND
- C1109 pad 1: /Power/FlyBuck/+24V -> +24V
- C1109 pad 2: /Power/FlyBuck/GND -> GND
- C1110 pad 1: /Power/FlyBuck/+24V -> +24V
- C1110 pad 2: /Power/FlyBuck/GND -> GND
- C1111 pad 1: /Power/FlyBuck/+24V -> +24V
- C1111 pad 2: /Power/FlyBuck/GND -> GND
- C1112 pad 1: /Power/FlyBuck/+24V -> +24V
- C1112 pad 2: GND_ISO -> /Power/GND_ISO
- C1113 pad 1: /Power/FlyBuck/+24V -> GND
- C1113 pad 2: GND_ISO -> Earth
- C1114 pad 1: /Power/FlyBuck/A -> +24V
- C1114 pad 2: /Power/FlyBuck/FB -> /Power/GND_ISO
- C1115 pad 2: GND_ISO -> /Power/FlyBuck/FB
- C301 pad 1: +POE -> +24V
- C301 pad 2: GND_ISO -> GND
- C302 pad 1: +POE -> +5V
- C302 pad 2: GND_ISO -> GND
- C303 pad 1: +POE -> +24V
- C303 pad 2: GND_ISO -> GND
- C304 pad 1: +POE -> +24V
- C304 pad 2: GND_ISO -> GND
- C306 pad 1: Net-(U301-BOOT) -> +24V
- C306 pad 2: Net-(D305-K) -> GND
- C307 pad 1: Net-(U301-COMP) -> +24V
- C307 pad 2: GND_ISO -> GND
- C308 pad 1: Net-(C308-Pad1) -> Net-(U301-SW)
- C308 pad 2: GND_ISO -> Net-(U301-BST)
- C309 pad 1: +5V_ISO -> +24V
- C309 pad 2: GND_ISO -> GND
- C310 pad 1: +5V_ISO -> +24V
- C310 pad 2: GND_ISO -> GND
- C311 pad 1: +5V_ISO -> GND
- C311 pad 2: GND_ISO -> +3.3V
- C312 pad 1: +5V -> +3.3V
- C313 pad 1: +5V -> Net-(U303-BOOT)
- C313 pad 2: GND -> Net-(D307-K)
- C314 pad 1: +3.3V -> Net-(U303-COMP)
- C501 pad 1: +5V_ISO -> +5V
- C501 pad 2: GND_ISO -> GND
- C503 pad 1: unconnected-(C503-Pad1) -> +3.3V
- C504 pad 1: +3.3V -> unconnected-(C504-Pad1)
- C512 pad 1: Net-(D502B-K1A2) -> +3.3V
- C513 pad 1: Net-(D502B-K1A2) -> +3.3V
- C513 pad 2: Net-(D502A-K3A4) -> GND
- C514 pad 1: Net-(D502A-K3A4) -> Net-(D502B-K1A2)
- C515 pad 1: Net-(D503B-K1A2) -> Net-(D502B-K1A2)
- C515 pad 2: GND -> Net-(D502A-K3A4)
- C516 pad 1: Net-(D503B-K1A2) -> Net-(D502A-K3A4)
- C516 pad 2: Net-(D503A-K3A4) -> GND
- C517 pad 1: Net-(D503A-K3A4) -> Net-(D503B-K1A2)
- C518 pad 1: Net-(D504B-K1A2) -> Net-(D503B-K1A2)
- C518 pad 2: GND -> Net-(D503A-K3A4)
- C519 pad 1: Net-(D504B-K1A2) -> Net-(D503A-K3A4)
- C519 pad 2: Net-(D504A-K3A4) -> GND
- C520 pad 1: Net-(D504A-K3A4) -> Net-(D504B-K1A2)
- C521 pad 1: Net-(D505B-K1A2) -> Net-(D504B-K1A2)
- C521 pad 2: GND -> Net-(D504A-K3A4)
- C522 pad 1: Net-(D505B-K1A2) -> Net-(D504A-K3A4)
- C522 pad 2: Net-(D505A-K3A4) -> GND
- C523 pad 1: Net-(D505A-K3A4) -> Net-(D505B-K1A2)
- C601 pad 1: +5V_ISO -> +3.3V
- C601 pad 2: GND_ISO -> GND
- C603 pad 1: Net-(U601-+Vout) -> +3.3V
- C604 pad 1: /frontend_420/+5V -> +3.3V
- C605 pad 1: /frontend_420/+5V -> +3.3V
- C606 pad 1: /frontend_420/+5V -> +3.3V
- C607 pad 1: /frontend_420/+5V -> +3.3V
- C608 pad 1: /frontend_420/+5V -> +3.3V
- C609 pad 1: /frontend_420/+5V -> GND
- C609 pad 2: GND -> Net-(U601-AIN0)
- C610 pad 1: /frontend_420/+5V -> GND
- C610 pad 2: GND -> Net-(U602-AIN0)
- C611 pad 1: /frontend_420/+5V -> GND
- C611 pad 2: GND -> Net-(U603-AIN0)
- C612 pad 1: /frontend_420/+5V -> GND
- C612 pad 2: GND -> Net-(U604-AIN0)
- C903 pad 2: /Digital Input/GND_IN -> GND
- C904 pad 2: /Digital Input/GND_IN -> GND
- C905 pad 2: /Digital Input/GND_IN -> GND
- C906 pad 2: /Digital Input/GND_IN -> GND
- C909 pad 2: /Digital Input/GND_IN -> GND
- C910 pad 2: /Digital Input/GND_IN -> GND
- C911 pad 2: /Digital Input/GND_IN -> GND
- C912 pad 2: /Digital Input/GND_IN -> GND
- D1101 pad 1: /Power/FlyBuck/+24V -> +24V
- D1102 pad 1: /Power/FlyBuck/+24V -> +24V
- D301 pad 1: +POE -> GND
- D301 pad 2: /Ethernet/POE+12 -> /Power/V+
- D302 pad 1: +POE -> +24V
- D302 pad 2: /Ethernet/POE+45 -> /Power/V+
- D303 pad 2: -POE -> /Ethernet/POE+12
- D304 pad 2: /Power/V+ -> /Ethernet/POE+45
- D305 pad 1: Net-(D305-K) -> +POE
- D305 pad 2: GND_ISO -> -POE
- D306 pad 1: GND_ISO -> GND
- D307 pad 1: GND -> Net-(D307-K)
- D307 pad 2: Net-(D307-A) -> GND
- D601 pad 1: /frontend_420/+5V -> GND
- D601 pad 2: Net-(D601-A) -> +3.3V
- D602 pad 2: /frontend_420/+5V -> +3.3V
- D602 pad 5: /frontend_420/+5V -> +3.3V
- D603 pad 1: GND -> /frontend_420/4200
- D603 pad 2: /frontend_420/+5V -> GND
- D604 pad 1: /frontend_420/4200 -> /frontend_420/4201
- D605 pad 1: /frontend_420/4201 -> /frontend_420/4202
- D606 pad 1: /frontend_420/4202 -> /frontend_420/4203
- F601 pad 1: Net-(D602A-K3A4) -> Net-(D601A-K3A4)
- F602 pad 1: Net-(D602B-K1A2) -> Net-(D601B-K1A2)
- F603 pad 1: Net-(D603A-K3A4) -> Net-(D602A-K3A4)
- F604 pad 1: Net-(D603B-K1A2) -> Net-(D602B-K1A2)
- FB501 pad 1: Net-(U502-+Vout) -> Net-(U501-+Vout)
- J103 pad 1: /Digital Input/IN0 -> /Power Output/OUT0
- J103 pad 2: /Digital Input/IN1 -> /Power Output/OUT1
- J103 pad 3: /Digital Input/IN2 -> GND
- J103 pad 4: /Digital Input/IN3 -> GND
- J104 pad 1: /Digital Input/IN4 -> /Digital Input/IN0
- J104 pad 2: /Digital Input/IN5 -> /Digital Input/IN1
- J104 pad 3: /Digital Input/IN6 -> /Digital Input/IN2
- J104 pad 4: /Digital Input/IN7 -> /Digital Input/IN3
- J105 pad 1: /Digital Input/GND_IN -> /Digital Input/IN4
- J105 pad 2: /Digital Input/GND_IN -> /Digital Input/IN5
- J106 pad 1: /frontend_temp/TC0+ -> GND
- J106 pad 2: /frontend_temp/TC0- -> GND
- J107 pad 1: /frontend_temp/TC2+ -> /Digital Output/OUT0
- J107 pad 2: /frontend_temp/TC2- -> /Digital Output/OUT1
- J107 pad 3: /frontend_temp/TC3+ -> /Digital Output/OUT2
- J107 pad 4: /frontend_temp/TC3- -> /Digital Output/OUT3
- J108 pad 1: VS -> /Digital Output/OUT4
- J108 pad 2: GND -> /Digital Output/OUT5
- J109 pad 1: /Digital Output/OUT0 -> /frontend_420/4200
- J109 pad 2: /Digital Output/OUT1 -> /frontend_420/4201
- J109 pad 3: /Digital Output/OUT2 -> /frontend_420/4202
- J109 pad 4: /Digital Output/OUT3 -> /frontend_420/4203
- J111 pad 1: /frontend_420/4200 -> /frontend_temp/TC0+
- J111 pad 2: /frontend_420/4201 -> /frontend_temp/TC0-
- J111 pad 3: /frontend_420/4202 -> /frontend_temp/TC1+
- J111 pad 4: /frontend_420/4203 -> /frontend_temp/TC1-
- J112 pad 1: /frontend_420/420_GND -> /frontend_temp/TC2+
- J112 pad 2: /frontend_420/420_GND -> /frontend_temp/TC2-
- L1101 pad 2: (no net) -> unconnected-(L1101-Pad2)
- L1101 pad 4: /Power/FlyBuck/GND -> GND
- L1101 pad 6: /Power/FlyBuck/GND -> GND
- L1101 pad 7: (no net) -> unconnected-(L1101-Pad7)
- L1101 pad 8: /Power/FlyBuck/+24V -> +24V
- L301 pad 1: Net-(D305-K) -> Net-(U301-SW)
- L301 pad 2: +5V_ISO -> +3.3V
- Q1001 pad 1: /Digital Output/~{EN} -> /EN
- Q1001 pad 3: /Digital Output/P00 -> /Digital Output/~{EN}
- Q1002 pad 3: /Digital Output/P06 -> /Digital Output/P00
- Q1003 pad 3: /Digital Output/P01 -> /Digital Output/P04
- Q1004 pad 3: /Digital Output/P07 -> /Digital Output/P01
- Q1005 pad 3: /Digital Output/P02 -> /Digital Output/P05
- Q1006 pad 3: /Digital Output/P03 -> /Digital Output/P02
- Q1007 pad 3: /Digital Output/P04 -> /Digital Output/P06
- Q1008 pad 3: /Digital Output/P05 -> /Digital Output/P03
- R1001 pad 1: /Digital Output/~{EN} -> GND
- R1001 pad 2: +3.3V -> /EN
- R1002 pad 1: GND -> /Digital Output/~{EN}
- R1002 pad 2: Net-(U1004-A1) -> +3.3V
- R1003 pad 2: /Digital Output/+5V -> +3.3V
- R1004 pad 2: /Digital Output/+5V -> +3.3V
- R1005 pad 2: Net-(U1004-A2) -> Net-(U1001-A2)
- R1006 pad 2: Net-(U1004-A0) -> Net-(U1001-A1)
- R1007 pad 1: Net-(U1004-~{INT}) -> GND
- R1007 pad 2: /Digital Output/+5V -> Net-(U1001-A0)
- R1008 pad 1: GND -> Net-(U1001-~{INT})
- R1008 pad 2: Net-(U1005-CL) -> +3.3V
- R1009 pad 1: /Digital Output/+5V -> GND
- R1009 pad 2: Net-(U1005-DIAG_EN) -> Net-(U1002-CL)
- R1010 pad 1: GND -> +3.3V
- R1010 pad 2: Net-(U1005-THER) -> Net-(U1002-DIAG_EN)
- R1011 pad 2: Net-(U1006-CL) -> Net-(U1002-THER)
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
